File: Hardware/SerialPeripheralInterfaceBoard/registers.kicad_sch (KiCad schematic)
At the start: 3 parts, among them U4 74HC04, U8 74HC165, U9 74HC595

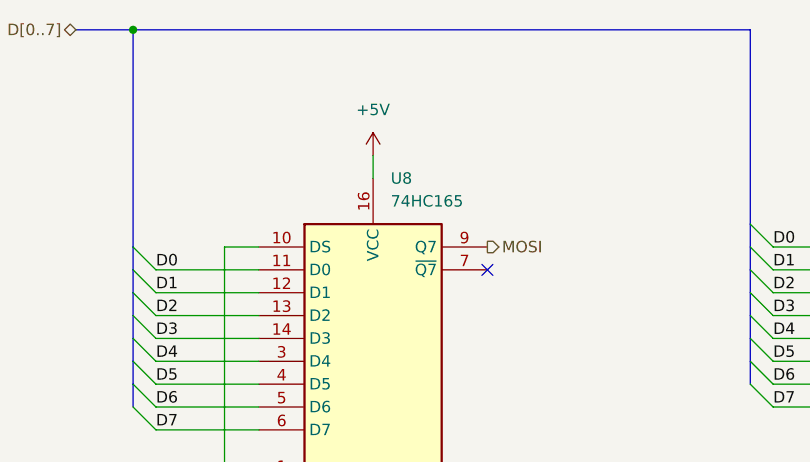
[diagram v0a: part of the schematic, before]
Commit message: feat: modify mother board for paging and dma
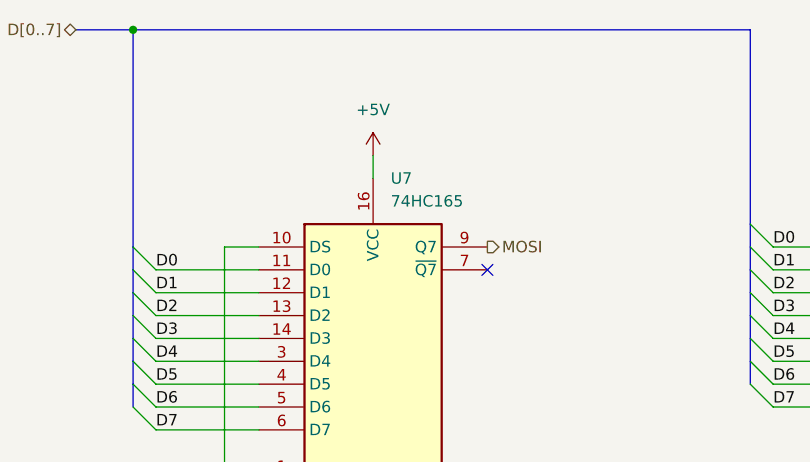
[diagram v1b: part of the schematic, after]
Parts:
- renumbered U8 to U7
